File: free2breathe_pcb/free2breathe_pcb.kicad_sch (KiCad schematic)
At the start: 33 parts

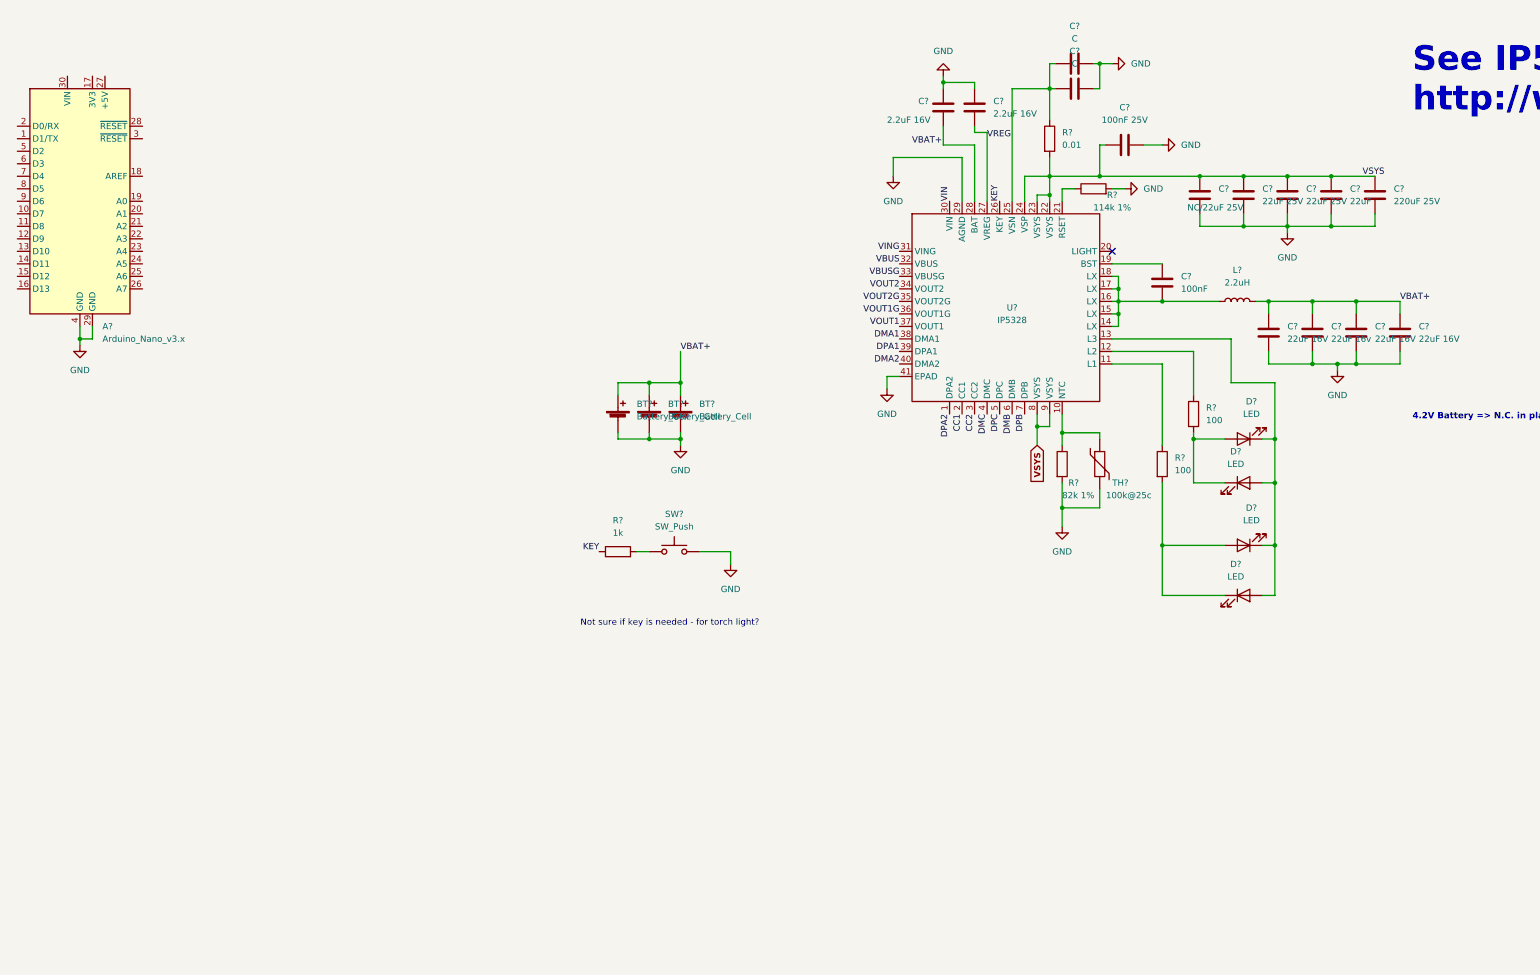
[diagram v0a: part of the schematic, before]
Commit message: update README, add USB-C connector to schematic
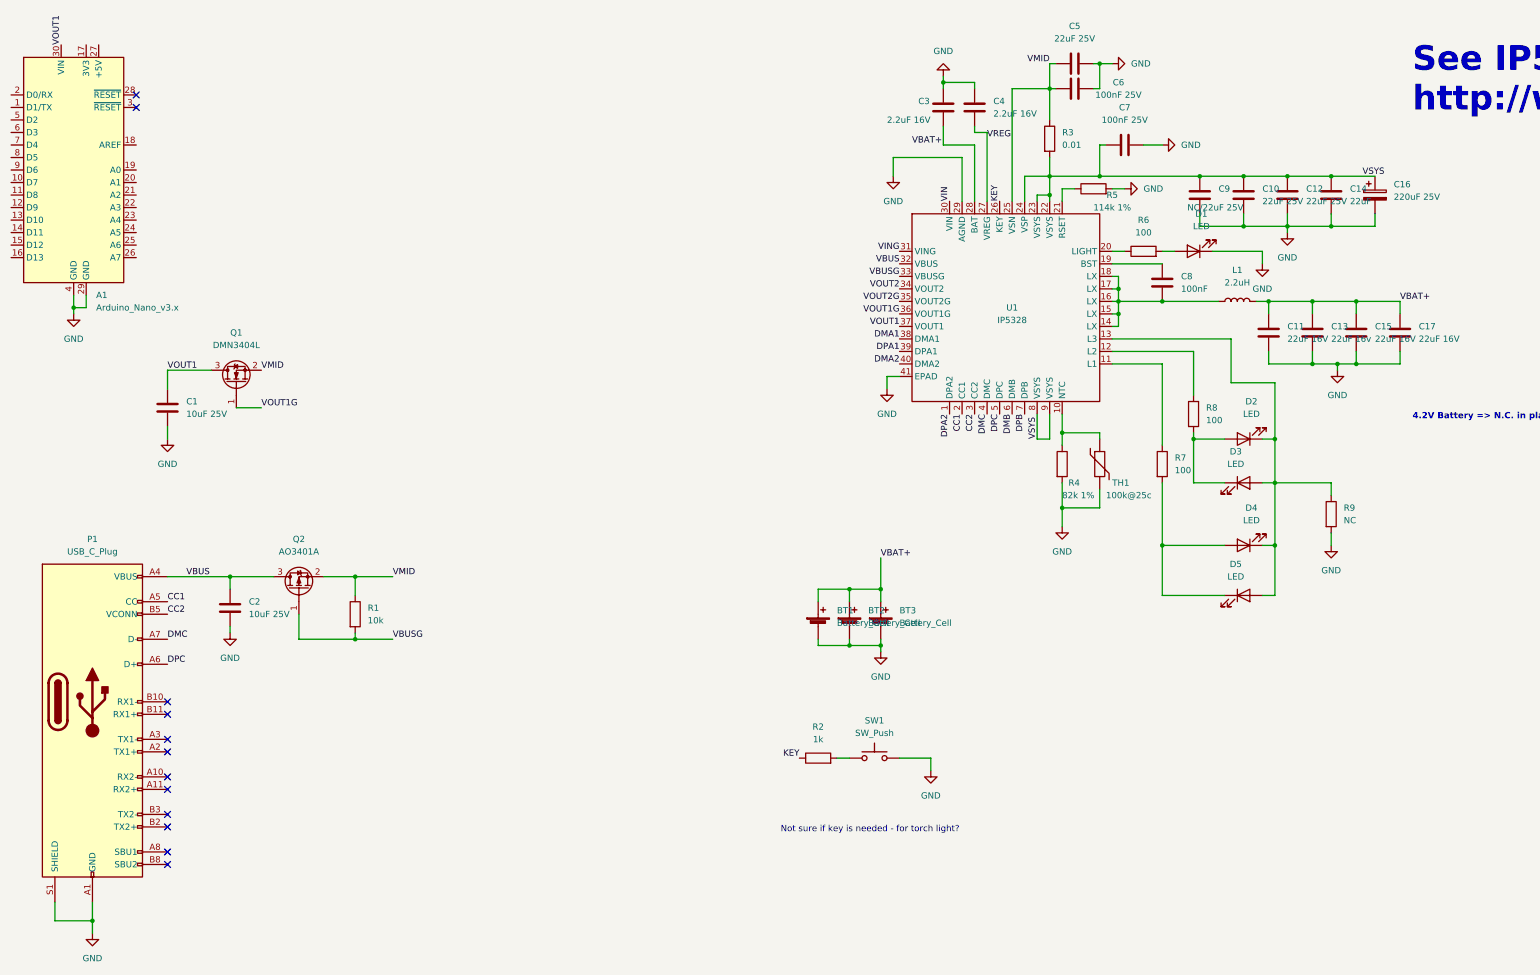
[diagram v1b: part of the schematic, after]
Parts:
- removed C?: 220uF 25V, symbol Device:C
- added C1, C2: 10uF 25V, symbol Device:C
- added C16: 220uF 25V, symbol Device:C_Polarized
- added D1: LED, symbol Device:LED
- added P1: USB_C_Plug, symbol Connector:USB_C_Plug
- added Q1: DMN3404L, Package_TO_SOT_SMD:SOT-23, symbol Transistor_FET:DMN3404L
- added Q2: AO3401A, Package_TO_SOT_SMD:SOT-23, symbol Transistor_FET:AO3401A
- added R1: 10k, symbol Device:R
- added R6: 100, symbol Device:R
- added R9: NC, symbol Device:R
- C5: renamed from C?; value C -> 22uF 25V
- C6: renamed from C?; value C -> 100nF 25V
- gave numbers to parts that had none: 30
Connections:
- net CC1: now also P1.A5 (CC)
- net CC2: now also P1.B5 (VCONN)
- net DMC: now also P1.A7 (D-)
- net DPC: now also P1.A6 (D+)
- net GND: now also C1.2, C16.2, C2.2, D1.1 (K), P1.A1 (GND), P1.A12 (GND), P1.B1 (GND), P1.B12 (GND), P1.S1 (SHIELD), R9.2
- net VBUS: now also C2.1, P1.A4 (VBUS), P1.A9 (VBUS), P1.B4 (VBUS), P1.B9 (VBUS), Q2.3 (D)
- net VBUSG: now also Q2.1 (G), R1.2
- net VOUT1: now also A1.30 (VIN), C1.1, Q1.3 (D)
- net VOUT1G: now also Q1.1 (G)
- net VSYS: now also C16.1
- net at D2.1 (K), D3.2 (A), D4.1 (K)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: now also R9.1
- net VMID: now reaches C5.2, C6.2, R3.1, U1.25 (VSN)
- net VMID: now also Q1.2 (S), Q2.2 (S), R1.1
- net at U1.20 (LIGHT): now also R6.1
- new net: D1.2 (A), R6.2
- no-connect marks 1 -> 12
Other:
- moved on the sheet: A1, BT1, BT2, BT3, R2, SW1

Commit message: add additional components, symbols and footprints
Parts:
- removed BT1, BT2: Battery_Cell, symbol Device:Battery_Cell
- removed P1: USB_C_Plug, symbol Connector:USB_C_Plug
- removed SW1: SW_Push, symbol Switch:SW_Push
- added J1: LED_Connector, Connector_JST:JST_PH_B2B-PH-K_1x02_P2.00mm_Vertical, symbol Connector:Conn_01x02_Female
- added J2: Alarm_Connector, alarm:AT_1127_ST_2_R_Alarm, symbol Connector:Conn_01x02_Female
- added P1: USB_C_Plug_USB2.0, symbol Connector:USB_C_Plug_USB2.0
- added R10, R12, R14, R16, R17, R18, R19, R20: 10k, Resistor_SMD:R_0603_1608Metric, symbol Device:R
- added R11, R13, R15: 100k, Resistor_SMD:R_0603_1608Metric, symbol Device:R
- added U2: CO Sensor, components:XDCR_110-102, symbol 110-102:110-102
- added U3: O3 Sensor, components:XDCR_110-102, symbol 110-102:110-102
- added U4: NO2 Sensor, components:XDCR_110-102, symbol 110-102:110-102
- added U5: SO2 Sensor, components:XDCR_110-102, symbol 110-102:110-102
- C1, C10, C11, C12, C13, C15, C16, C17, C2, C3, C4, C5, C6, C7, C9: footprint (none) -> Capacitor_SMD:C_0201_0603Metric
- C14: value 22uF -> 22uF 25V; footprint (none) -> Capacitor_SMD:C_0201_0603Metric
- C8: value 100nF -> 100nF 25V; footprint (none) -> Capacitor_SMD:C_0201_0603Metric
- R1, R3, R4, R5, R6, R7, R8, R9: footprint (none) -> Resistor_SMD:R_0603_1608Metric
- R2: value 1k -> 100k; footprint (none) -> Resistor_SMD:R_0603_1608Metric
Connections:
- net CC1: now also P1.A5 (CC)
- net CC2: now also P1.B5 (VCONN)
- net DMC: now also P1.A7 (D-)
- net DPC: now also P1.A6 (D+)
- net GND: now also J1.1 (Pin_1), J2.2 (Pin_2), P1.A1 (GND), P1.A12 (GND), P1.B1 (GND), P1.B12 (GND), P1.S1 (SHIELD), R10.2, R12.2, R14.2, R16.2
- net VBUS: now also P1.A4 (VBUS), P1.A9 (VBUS), P1.B4 (VBUS), P1.B9 (VBUS)
- net Arduino_A1: now reaches R2.2
- net Arduino_A1: now also A1.20 (A1), R10.1, R17.1, U2.1 (WORKING), U2.6 (WORKING)
- net Arduino_D8: now reaches A1.11 (D8)
- net Arduino_D8: now also J1.2 (Pin_2)
- net Arduino_D9: now reaches A1.12 (D9)
- net Arduino_D9: now also J2.1 (Pin_1)
- net Arduino_3V3: now reaches A1.17 (3V3)
- net Arduino_3V3: now also R2.1, R11.1, R13.1, R15.1
- net Arduino_A0: now reaches A1.19 (A0)
- net Arduino_A0: now also R17.2, U2.4 (REFERENCE), U2.5 (COUNTER)
- net Arduino_A2: now reaches A1.21 (A2)
- net Arduino_A2: now also R18.1, U3.4 (REFERENCE), U3.5 (COUNTER)
- net Arduino_A3: now reaches A1.22 (A3)
- net Arduino_A3: now also R11.2, R12.1, R18.2, U3.1 (WORKING), U3.6 (WORKING)
- net Arduino_A4: now reaches A1.23 (A4)
- net Arduino_A4: now also R19.1, U4.4 (REFERENCE), U4.5 (COUNTER)
- net Arduino_A5: now reaches A1.24 (A5)
- net Arduino_A5: now also R13.2, R14.1, R19.2, U4.1 (WORKING), U4.6 (WORKING)
- net Arduino_A6: now reaches A1.25 (A6)
- net Arduino_A6: now also R20.1, U5.4 (REFERENCE), U5.5 (COUNTER)
- net Arduino_A7: now reaches A1.26 (A7)
- net Arduino_A7: now also R15.2, R16.1, R20.2, U5.1 (WORKING), U5.6 (WORKING)
- net KEY: no longer names the net of U1.26 (KEY)
- net KEY: no longer R2.1
- no-connect marks 12 -> 3
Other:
- note removed: "Not sure if key is needed - for torch light?"

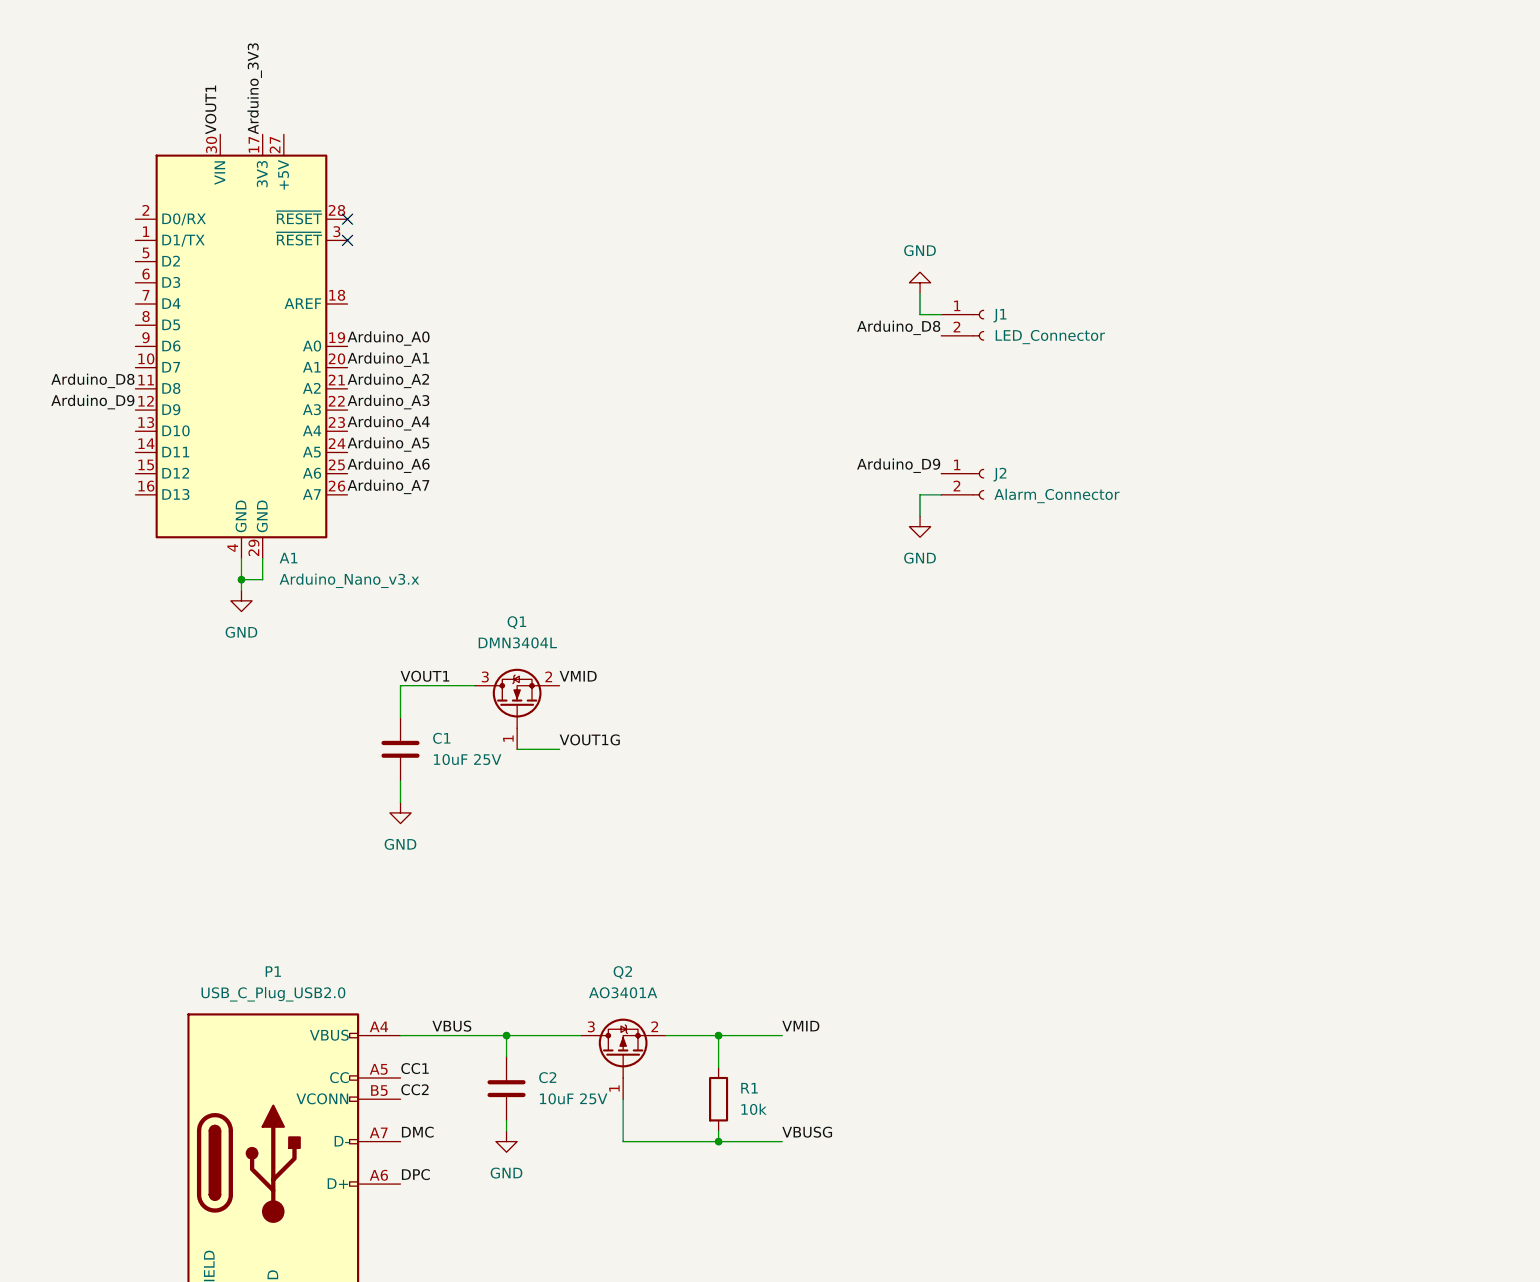
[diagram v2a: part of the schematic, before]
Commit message: add status LEDs and connectors
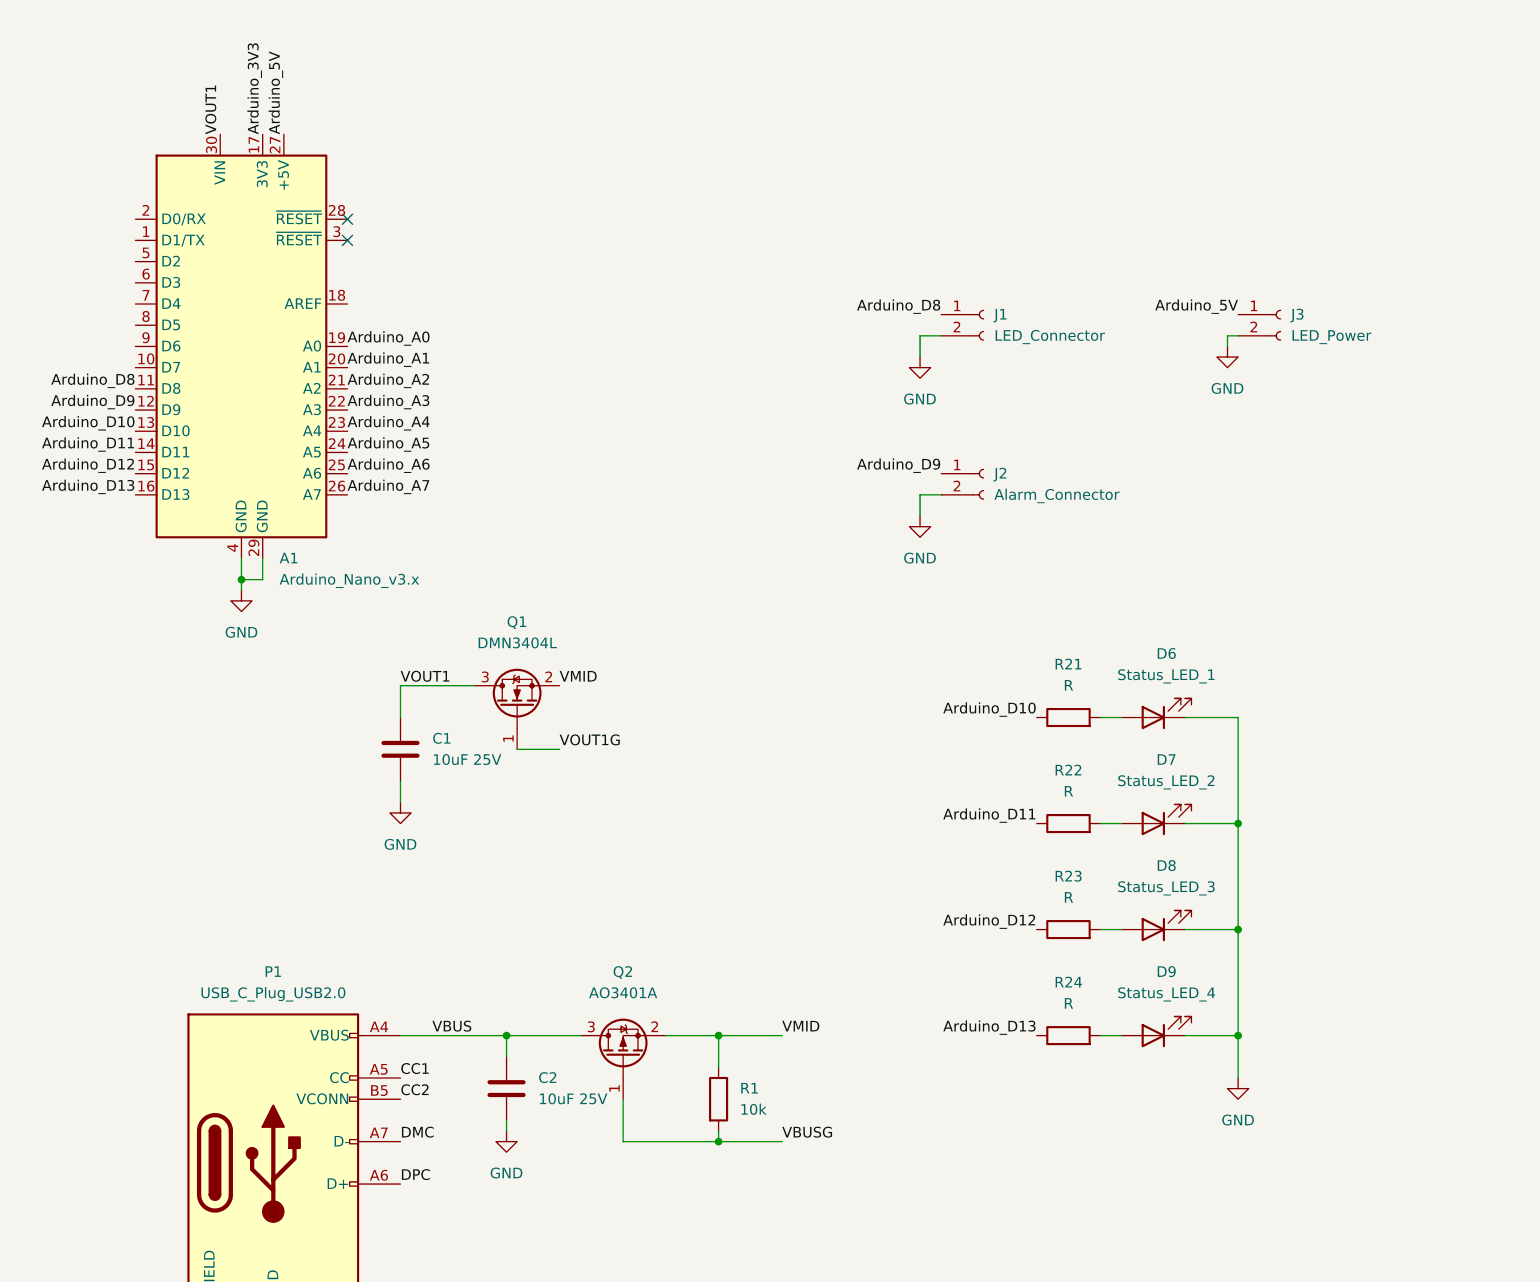
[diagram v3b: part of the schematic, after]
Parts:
- added D6: Status_LED_1, symbol Device:LED
- added D7: Status_LED_2, symbol Device:LED
- added D8: Status_LED_3, symbol Device:LED
- added D9: Status_LED_4, symbol Device:LED
- added J3: LED_Power, symbol Connector:Conn_01x02_Female
- added R21, R22, R23, R24: R, symbol Device:R
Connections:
- net Arduino_D8: now also J1.1 (Pin_1); no longer J1.2 (Pin_2)
- net GND: now also J1.2 (Pin_2), D6.1 (K), D7.1 (K), D8.1 (K), D9.1 (K), J3.2 (Pin_2); no longer J1.1 (Pin_1)
- net Arduino_D10: now reaches A1.13 (D10)
- net Arduino_D10: now also R21.1
- net Arduino_D11: now reaches A1.14 (D11)
- net Arduino_D11: now also R22.1
- net Arduino_D12: now reaches A1.15 (D12)
- net Arduino_D12: now also R23.1
- net Arduino_D13: now reaches A1.16 (D13)
- net Arduino_D13: now also R24.1
- net Arduino_5V: now reaches A1.27 (+5V)
- net Arduino_5V: now also J3.1 (Pin_1)
- new net: D9.2 (A), R24.2
- new net: D6.2 (A), R21.2
- new net: D7.2 (A), R22.2
- new net: D8.2 (A), R23.2

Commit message: added switch to schematic
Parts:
- added SW1: SW_SPST, switch:switch_pad, symbol Switch:SW_SPST
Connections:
- net VBAT+: now also SW1.2 (B); no longer BT3.1 (+)
- new net: BT3.1 (+), SW1.1 (A)
